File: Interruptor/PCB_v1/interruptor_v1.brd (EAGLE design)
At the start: 100 x 80 mm, 0 parts

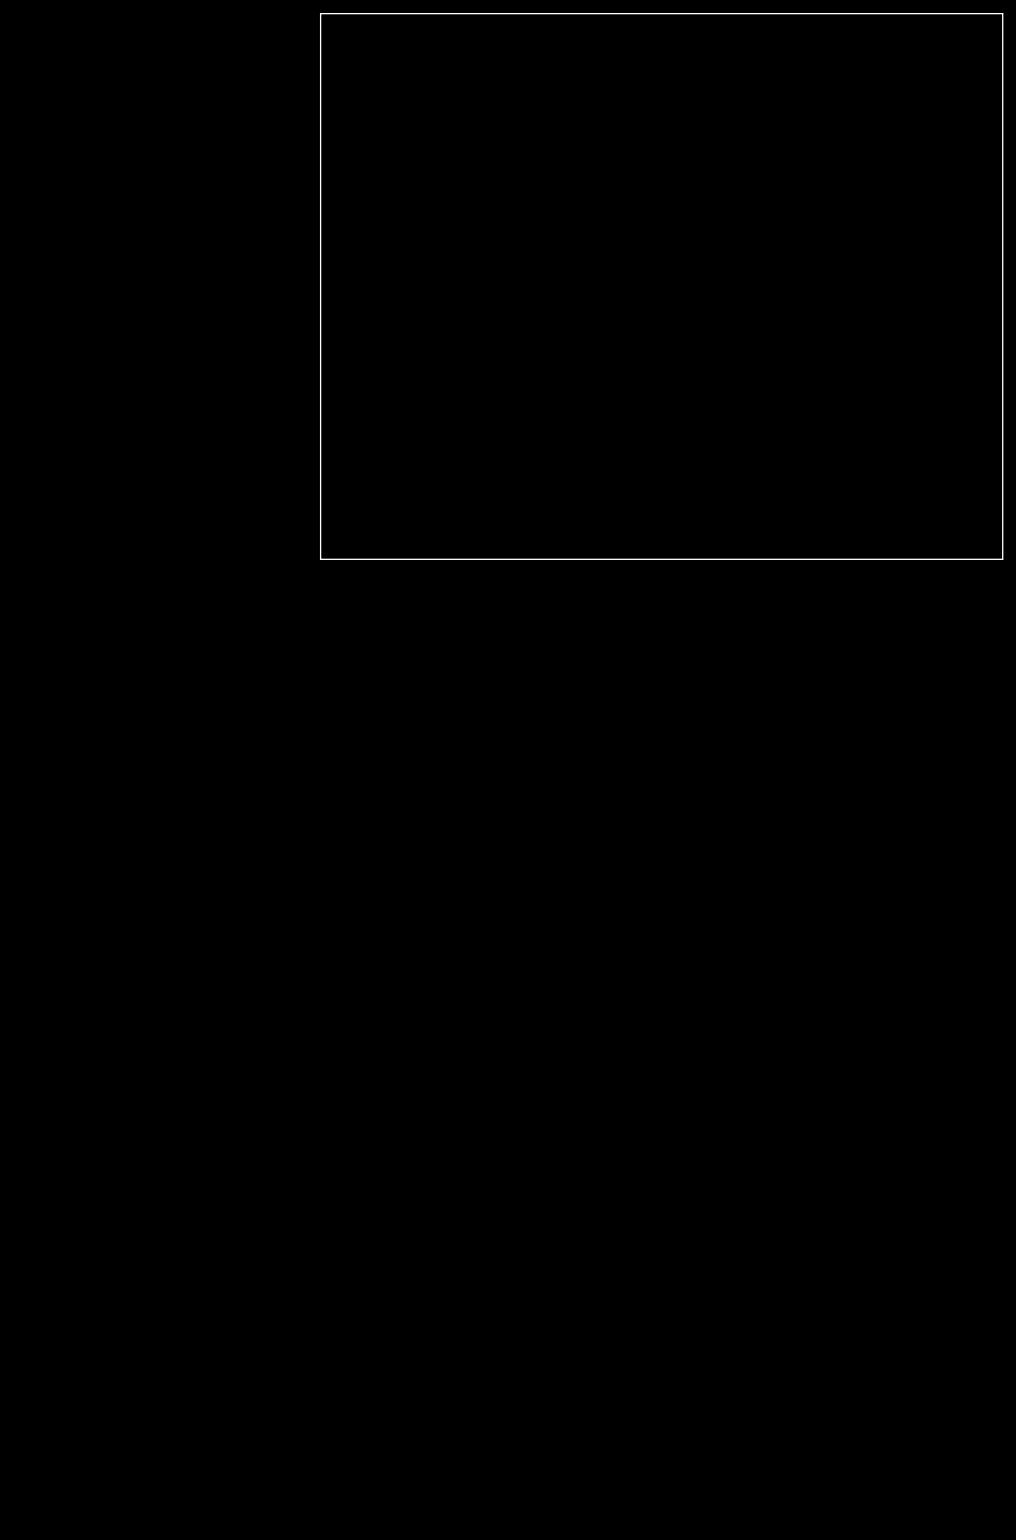
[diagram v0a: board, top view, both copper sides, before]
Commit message: Schematic of ZCD and MIDI
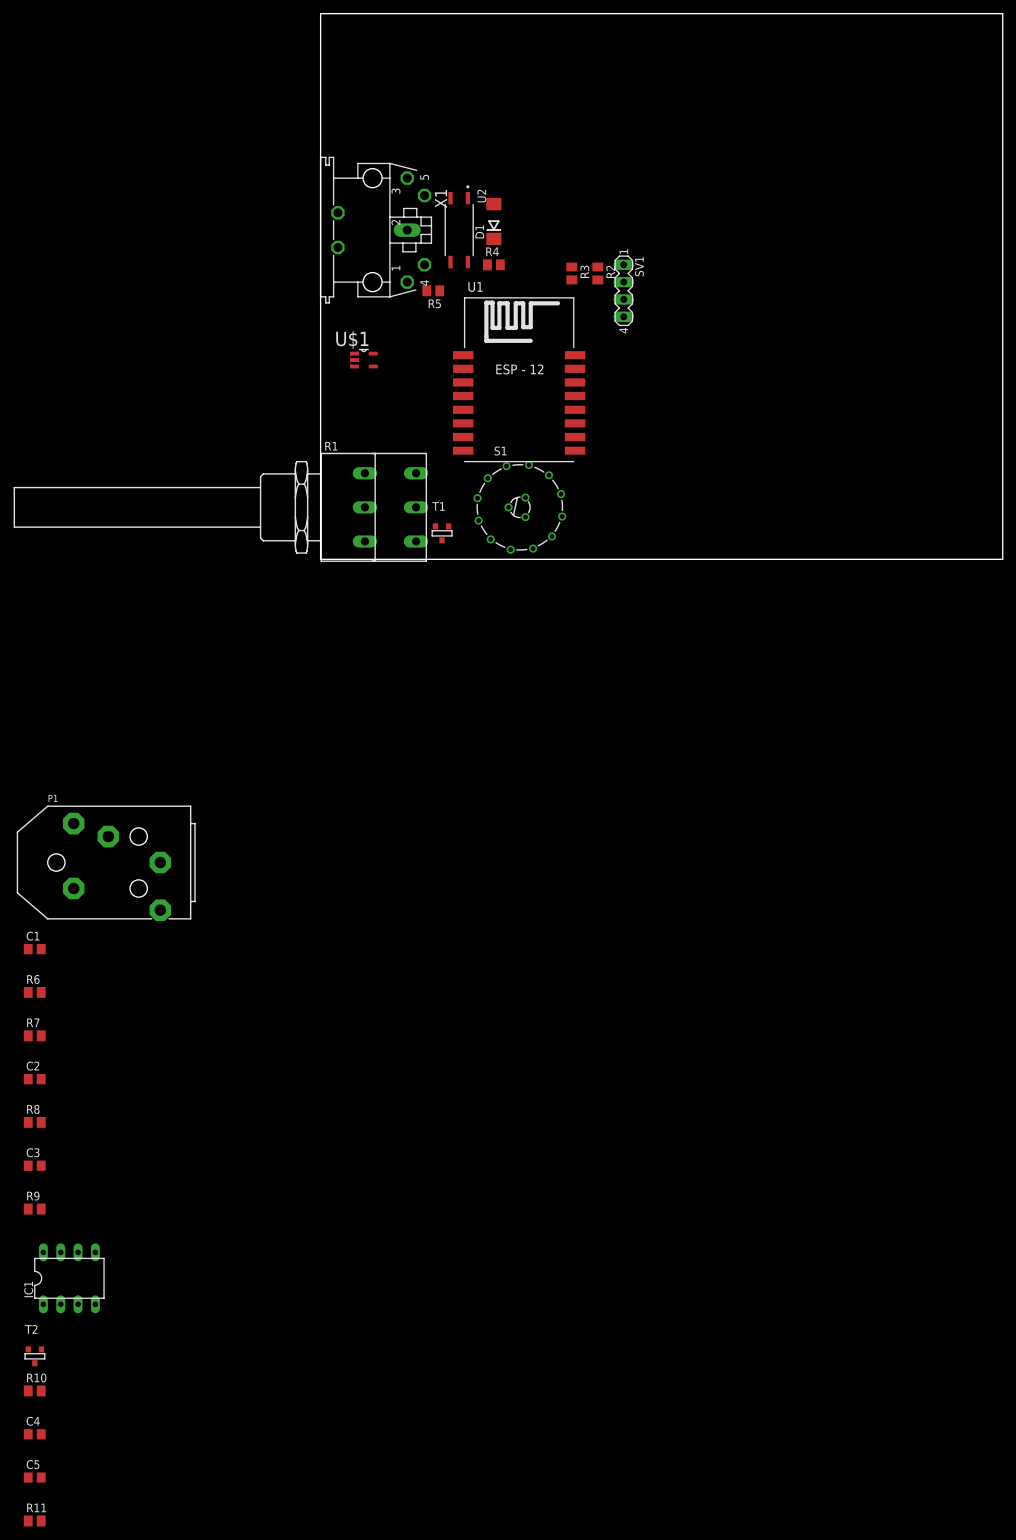
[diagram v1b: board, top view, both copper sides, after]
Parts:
- added C1: 10uF, rcl:C0805
- added C2, C4: 100nF, rcl:C0805
- added C3: 10nF, rcl:C0805
- added C5: ??, rcl:C0805
- added D1: (no value), diode:DO214AA
- added IC1: ICM7555, maxim:DIL08
- added P1: (no value), audio:PJ-RN
- added R1: PC16D, piher:PC16D
- added R10, R11, R6, R7, R9: 2.2k, resistor:M0805
- added R2, R3, R4: (no value), resistor:M0805
- added R5: 220, resistor:M0805
- added R8: 22k, resistor:M0805
- added S1: 50-3POLE30, switch:50-3POLE30
- added SV1: I2C, con-lstb:MA04-1
- added T1, T2: (no value), zetex:SOT-23
- added U$1: MCP6001RT-E/OT, MCP6001RT-E_OT:SOT95P270X145-5N
- added U1: (no value), esp8266modules:ESP12-SMD
- added U2: TCLD1000, TCLD1000:SOIC254P1020X230-4N
- added X1: MAB5SH, con-hirschmann:MAB5SH
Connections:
- new net 3V3: IC1.4, IC1.8, R1.1E, R1.1S, R1.2E, R10.1, R2.1, R3.1, R4.2, SV1.1, U$1.5, U1.CH_PD, U1.VCC
- new net ESP_TRIG_OUT: S1.5, S1.6, U1.GPIO2
- new net GND: C2.1, C4.1, C5.1, IC1.1, R1.2A, SV1.4, T2.2, U$1.2, U1.GND, U1.GPIO15, U2.3
- new net N$1: R4.1, U2.4
- new net N$10: C3.2, R7.1, R8.2, U$1.4
- new net N$11: IC1.2, R10.2, T2.1
- new net N$12: C3.1, R8.1, R9.2, U$1.1
- new net N$13: C4.2, IC1.5
- new net N$14: R9.1, T2.3
- new net N$16: C5.2, IC1.6, IC1.7, R1.1A
- new net N$18: IC1.3, S1.7
- new net N$2: R5.2, X1.4
- new net N$20: R11.1, S1.C2
- new net N$21: R11.2, T1.3
- new net N$3: D1.C, R5.1, U2.1
- new net N$4: D1.A, U2.2, X1.5
- new net N$5: R1.2S, U1.ADC
- new net N$6: C1.1, P1.TIP
- new net N$7: C2.2, P1.SLEEVE, R7.2
- new net N$8: C1.2, R6.2
- new net N$9: R6.1, U$1.3
- new net PE: X1.PE, X1.PE@
- new net PGM: U1.GPIO0
- new net RX: U1.RXD0
- new net SCL: R2.2, SV1.2, U1.GPIO4
- new net SDA: R3.2, SV1.3, U1.GPIO5

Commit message: Finished with 1/4
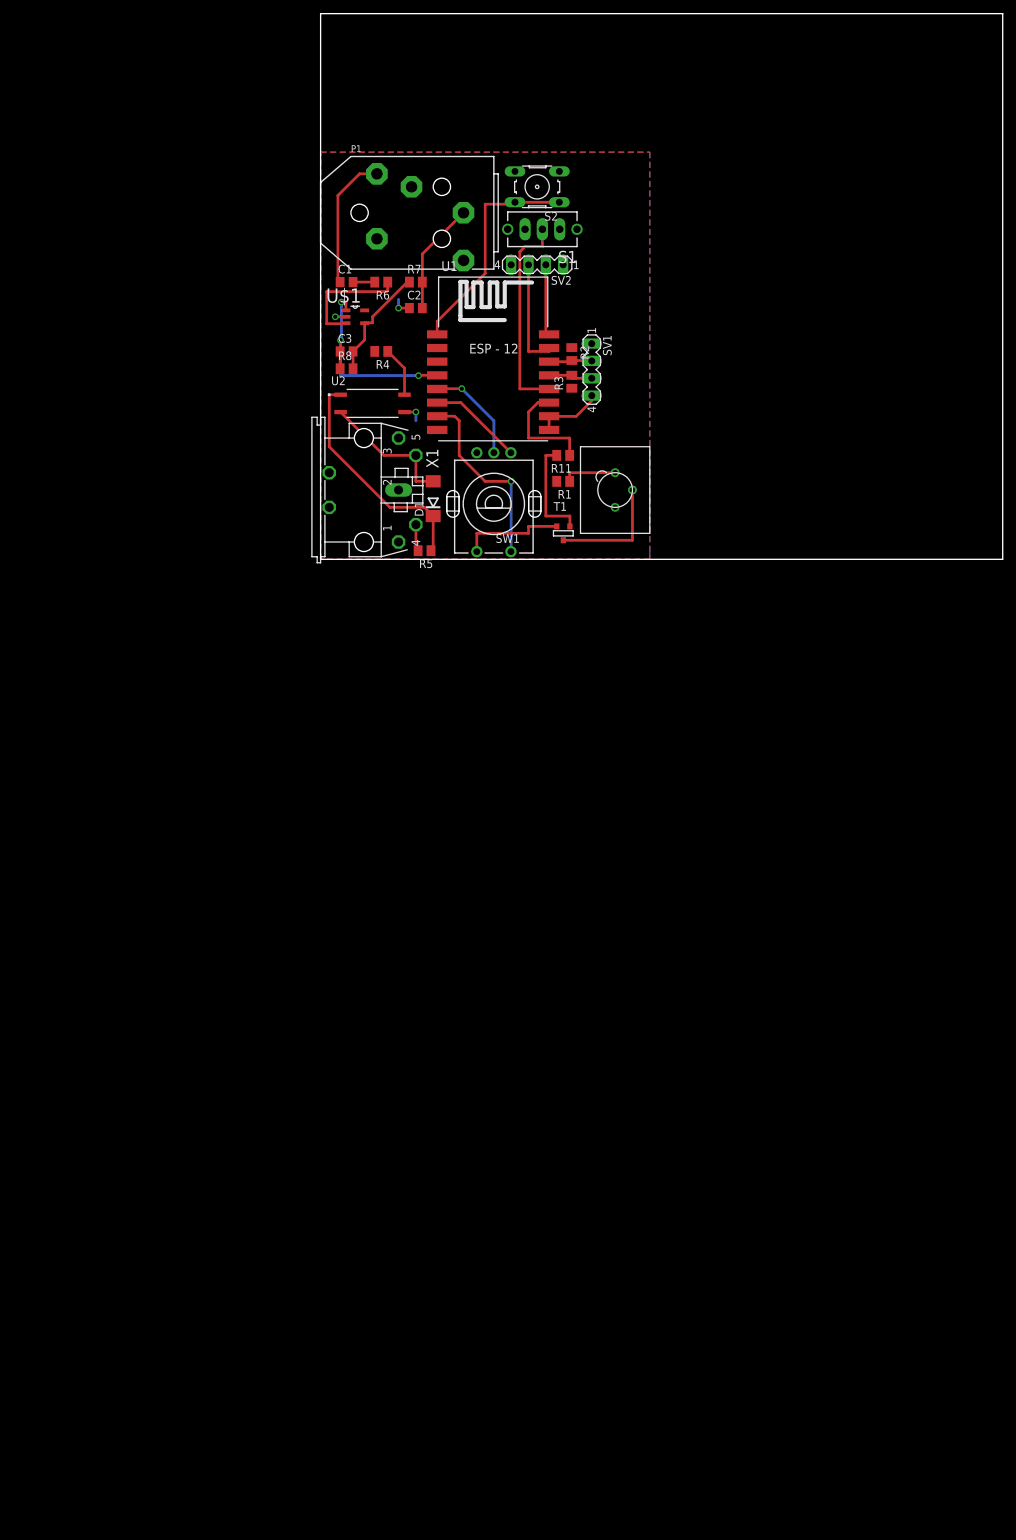
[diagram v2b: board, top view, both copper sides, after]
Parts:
- removed C4: 100nF, rcl:C0805
- removed C5: ??, rcl:C0805
- removed IC1: ICM7555, maxim:DIL08
- removed R10, R9: 2.2k, resistor:M0805
- removed T2: (no value), zetex:SOT-23
- added S2: Reset, switch-omron:B3F-10XX
- added SV2: UART, con-lstb:MA04-1
- added SW1: CI-11, piher:CI-11
- added U$2: OPF372OPF372, fibre:OPF372
- R1: value PC16D -> 15R 1/2W; device piher:PC16D -> resistor:M0805
- S1: value 50-3POLE30 -> Prog; device switch:50-3POLE30 -> switch:TL3XYO
- moved R11 174.4 mm to (35.6, 15.2), turned to 180 degrees
- moved C3 127.8 mm to (3.81, 30.5)
- moved C2 126.1 mm to (14.0, 36.8)
- moved R7 123.8 mm to (14.0, 40.6)
- moved R8 119.6 mm to (3.81, 27.9)
- moved R6 115.9 mm to (8.89, 40.6), turned to 180 degrees
- moved C1 107.9 mm to (3.81, 40.6)
- moved P1 105.1 mm to (17.8, 50.8)
- moved D1 41.6 mm to (16.5, 8.89)
- moved S1 40.9 mm to (32.5, 48.4), turned to 180 degrees
- moved R5 38.1 mm to (15.2, 1.27)
- moved X1 38.1 mm to (6.35, 10.2)
- moved R1 35.8 mm to (35.6, 11.4), turned to 180 degrees
- moved U2 28.4 mm to (7.62, 22.9), turned to 0 degrees
- moved R4 20.8 mm to (8.89, 30.5), turned to 180 degrees
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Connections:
- removed net N$18: IC1.3, S1.7
- removed net N$20: R11.1, S1.C2
- new net N$15: S2.1, S2.2, U1.RESET
- new net TX: SV2.2, U1.TXD0
- net 3V3: now also R1.2, SV2.1; no longer IC1.4, IC1.8, R1.1E, R1.1S, R1.2E, R10.1
- net ESP_TRIG_OUT: now also R11.1; no longer S1.5, S1.6
- net GND: now also S1.3, S2.3, S2.4, SV2.4, SW1.C, SW1.E, T1.2; no longer C4.1, C5.1, IC1.1, R1.2A, T2.2
- net N$11: now also SW1.A, U1.GPIO12; no longer IC1.2, R10.2, T2.1
- net N$12: now also U1.GPIO16; no longer R9.2
- net N$13: now also SW1.B, U1.GPIO14; no longer C4.2, IC1.5
- net N$14: now also T1.1, U$2.CATHODE; no longer R9.1, T2.3
- net N$16: now also R1.1, U$2.ANODE; no longer C5.2, IC1.6, IC1.7, R1.1A
- net N$5: now also SW1.D, U1.GPIO13; no longer R1.2S, U1.ADC
- net PGM: now also S1.2
- net RX: now also SV2.3
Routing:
- net N$3: track 0.00 -> 34.1 mm
- net N$15: track 0.00 -> 33.2 mm
- net GND: track 0.00 -> 33.1 mm, vias 0 -> 3
- net N$12: track 0.00 -> 31.3 mm, vias 0 -> 3
- net PGM: track 0.00 -> 30.6 mm
- net N$5: track 0.00 -> 28.1 mm, vias 0 -> 1
- net N$4: track 0.00 -> 20.0 mm
- net N$6: track 0.00 -> 19.9 mm
- net N$9: track 0.00 -> 17.8 mm
- net N$14: track 0.00 -> 17.5 mm
- net N$10: track 0.00 -> 17.0 mm
- net N$7: track 0.00 -> 16.5 mm
- net RX: track 0.00 -> 16.2 mm
- net ESP_TRIG_OUT: track 0.00 -> 16.0 mm
- net N$21: track 0.00 -> 15.5 mm
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- added copper zone on layer 1, net 3V3
- added copper zone on layer 16, net GND

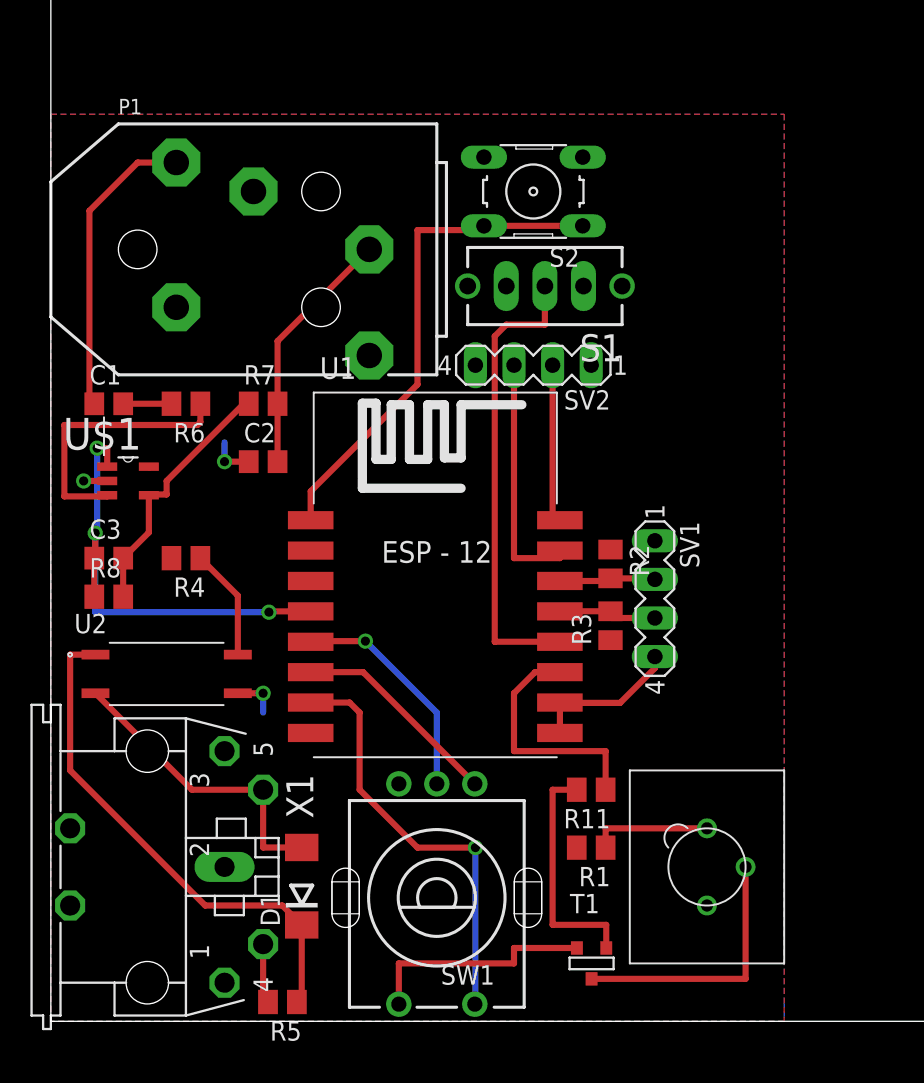
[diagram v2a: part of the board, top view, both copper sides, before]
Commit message: No DRC, now to route
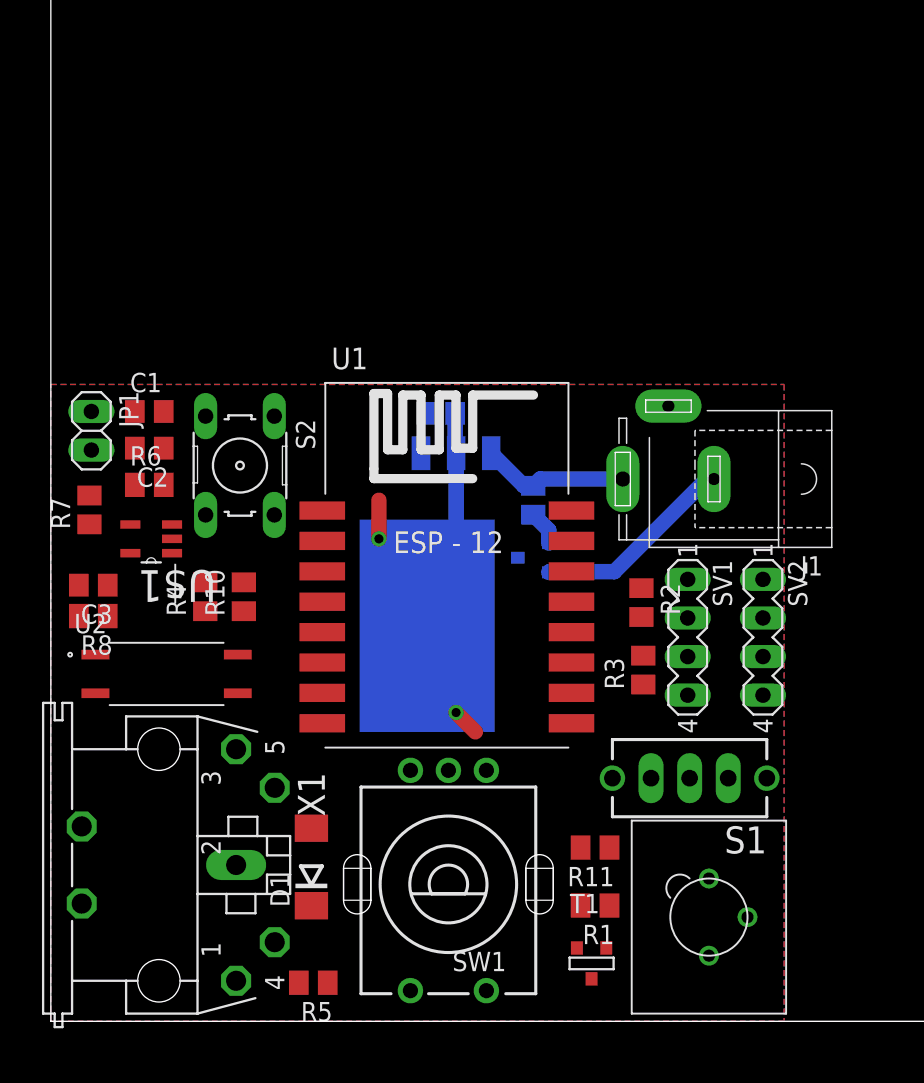
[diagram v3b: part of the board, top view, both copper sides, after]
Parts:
- removed P1: (no value), audio:PJ-RN
- added C4: 10uF, rcl:C0805
- added IC1: LM1117MPX-3.3, lm1117:SOT223
- added J1: (no value), con-jack:SPC4077
- added JP1: (no value), pinhead:1X02
- added R10: 4.7k, resistor:M0805
- added R9: 22k, resistor:M0805
- added T2: (no value), zetex:SOT-23
- R2, R3: value (none) -> 4.7k
- moved S1 33.8 mm to (42.0, 16.0)
- moved S2 26.4 mm to (12.4, 36.6), turned to 270 degrees
- moved SV2 23.4 mm to (46.9, 25.3), turned to 270 degrees
- moved R7 13.4 mm to (2.54, 33.7), turned to 90 degrees
- moved C2 7.55 mm to (6.48, 37.7), turned to 180 degrees
- moved R6 5.85 mm to (6.48, 35.3), turned to 0 degrees
- moved U$1 4.10 mm to (6.60, 31.8), turned to 180 degrees
- moved R11 3.82 mm to (35.8, 11.4)
- moved R1 3.82 mm to (35.8, 7.62)
- moved R3 3.63 mm to (39.0, 23.1)
- moved SV1 3.33 mm to (41.9, 25.3)
- moved U$2 3.30 mm to (43.3, 6.86)
- moved R2 3.25 mm to (38.9, 27.6)
- moved R4 2.84 mm to (10.2, 27.9), turned to 90 degrees
- moved C1 2.71 mm to (6.48, 40.1)
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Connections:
- new net N$17: J1.1, T2.2
- new net N$18: IC1.3, J1.3, R9.1
- new net N$19: R9.2, T2.3
- new net N$20: R10.1, U1.GPIO16
- net 3V3: now also C4.2, IC1.2, IC1.TAB
- net GND: now also C4.1, IC1.1, T2.1
- net N$12: now also R10.2; no longer U1.GPIO16
- net N$6: now also JP1.1; no longer P1.TIP
- net N$7: now also JP1.2; no longer P1.SLEEVE
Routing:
- net N$3: track 34.1 -> 0.00 mm
- net N$15: track 33.2 -> 0.00 mm
- net GND: track 33.1 -> 0.00 mm, vias 3 -> 0
- net N$12: track 31.3 -> 0.60 mm, vias 3 -> 0
- net PGM: track 30.6 -> 0.00 mm
- net 3V3: track 0.07 -> 29.4 mm, vias 0 -> 2
- net N$5: track 28.1 -> 0.00 mm, vias 1 -> 0
- net N$4: track 20.0 -> 0.00 mm
- net N$6: track 19.9 -> 0.00 mm
- net N$9: track 17.8 -> 0.00 mm
- net N$14: track 17.5 -> 0.00 mm
- net N$10: track 17.0 -> 0.00 mm
- net N$7: track 16.5 -> 0.00 mm
- net RX: track 16.2 -> 0.00 mm
- net ESP_TRIG_OUT: track 16.0 -> 0.00 mm
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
